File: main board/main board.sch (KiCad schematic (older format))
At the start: 1 part, among them J1 502078-1710

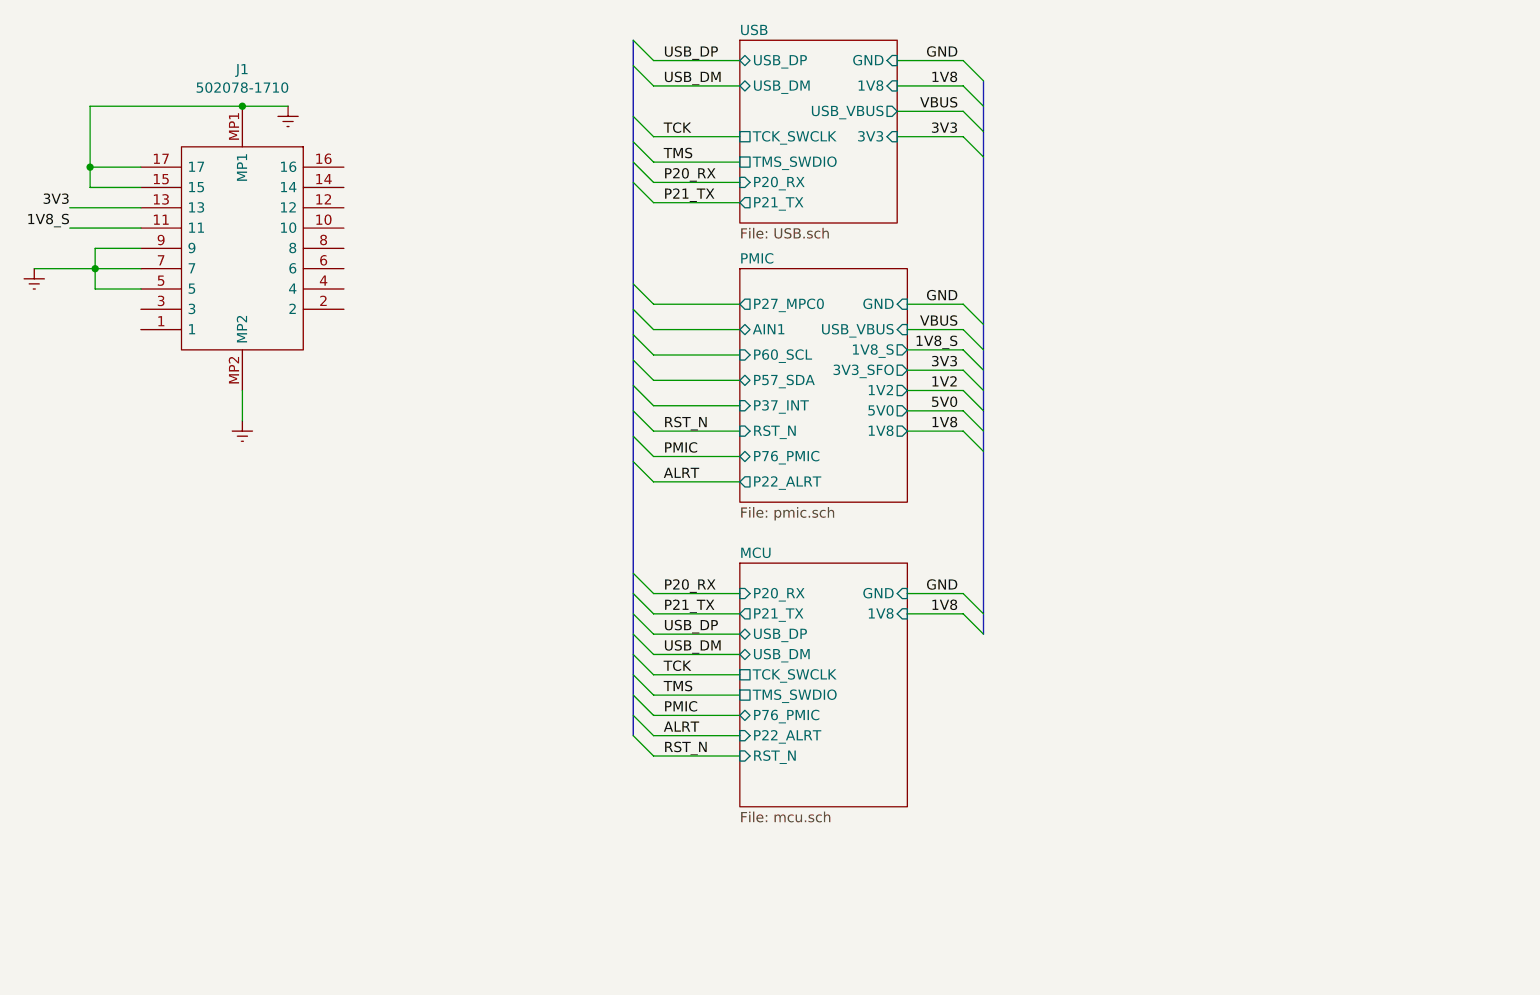
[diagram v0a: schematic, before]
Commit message: added crystal and motion sensor
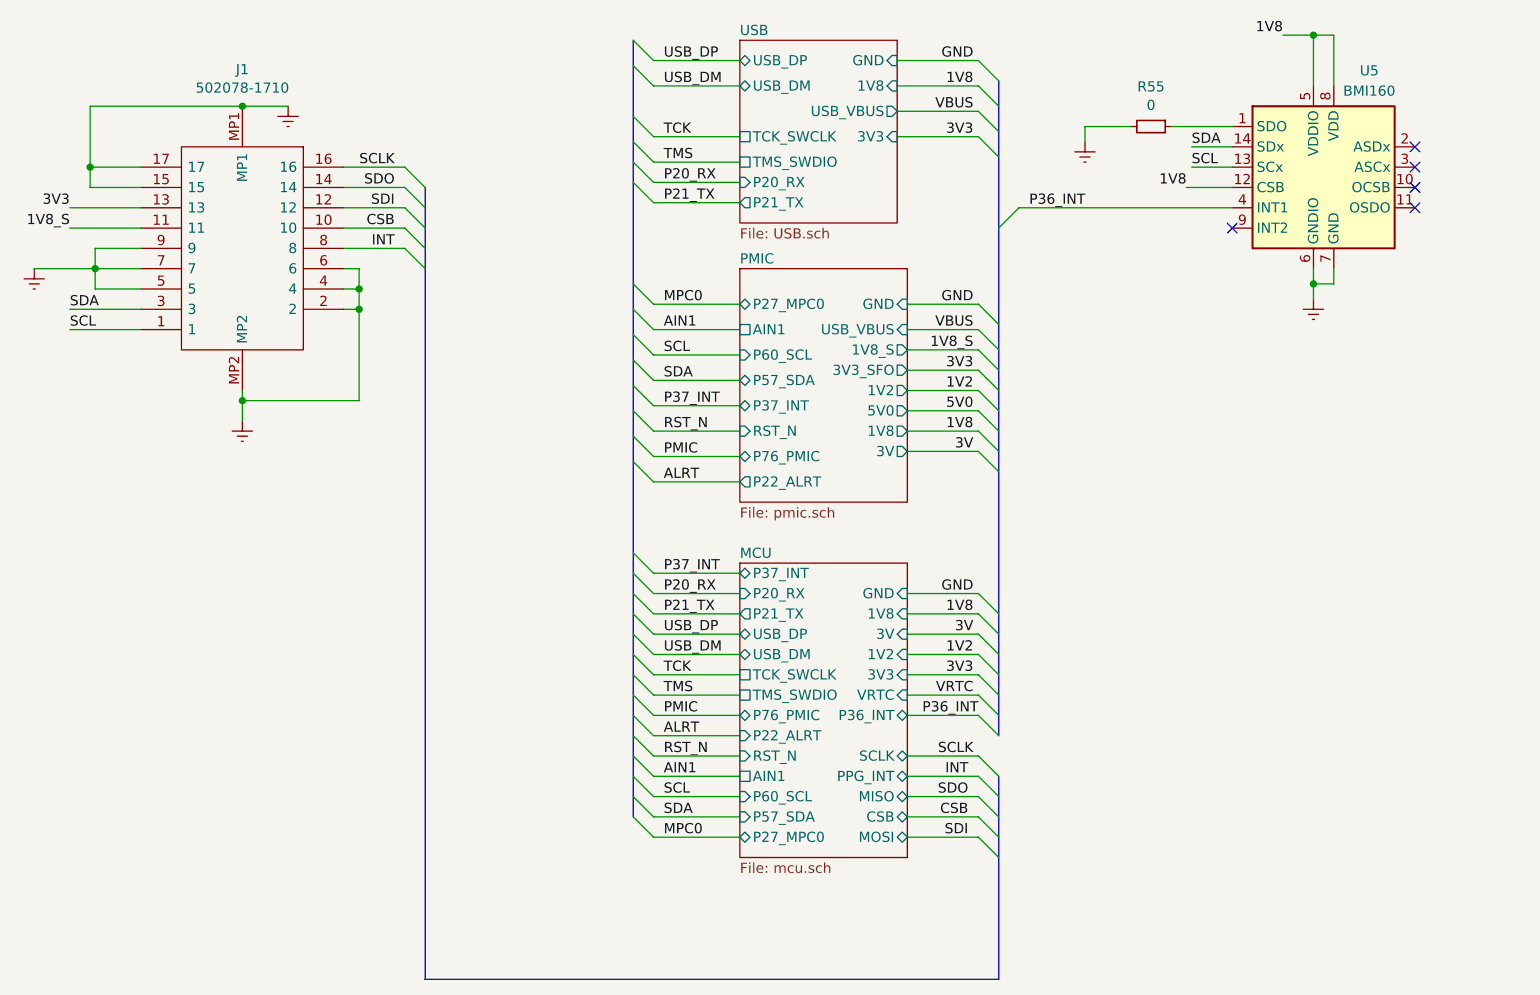
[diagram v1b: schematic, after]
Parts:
- added R55: 0, symbol Device:R_Small
- added U5: BMI160, Package_LGA:Bosch_LGA-14_3x2.5mm_P0.5mm, symbol Sensor_Motion:BMI160
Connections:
- net 1V8: now also U5.12 (CSB), U5.5 (VDDIO), U5.8 (VDD)
- net GNDREF: now also J1.2, J1.4, J1.6, R55.2, U5.6 (GNDIO), U5.7 (GND)
- net SCL: now reaches J1.1
- net SCL: now also U5.13 (SCx)
- net CSB: now reaches J1.10
- net SDI: now reaches J1.12
- net SDO: now reaches J1.14
- net SCLK: now reaches J1.16
- net SDA: now reaches J1.3
- net SDA: now also U5.14 (SDx)
- net INT: now reaches J1.8
- new net: R55.1, U5.1 (SDO)
- new net P36_INT: U5.4 (INT1)
- no-connect marks 0 -> 5

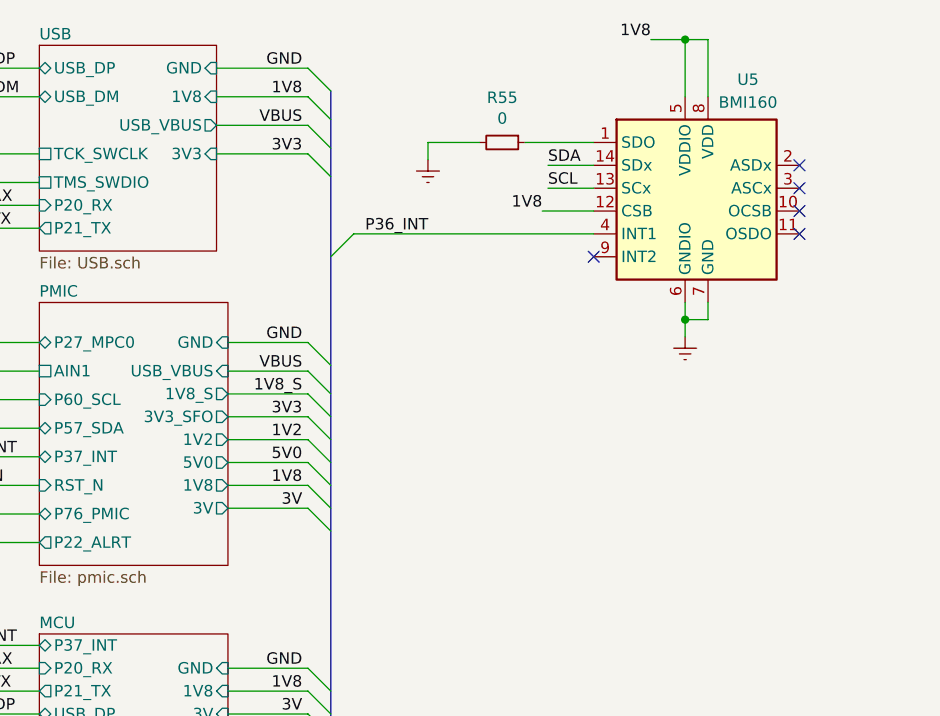
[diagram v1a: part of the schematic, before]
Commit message: added VRTC power input
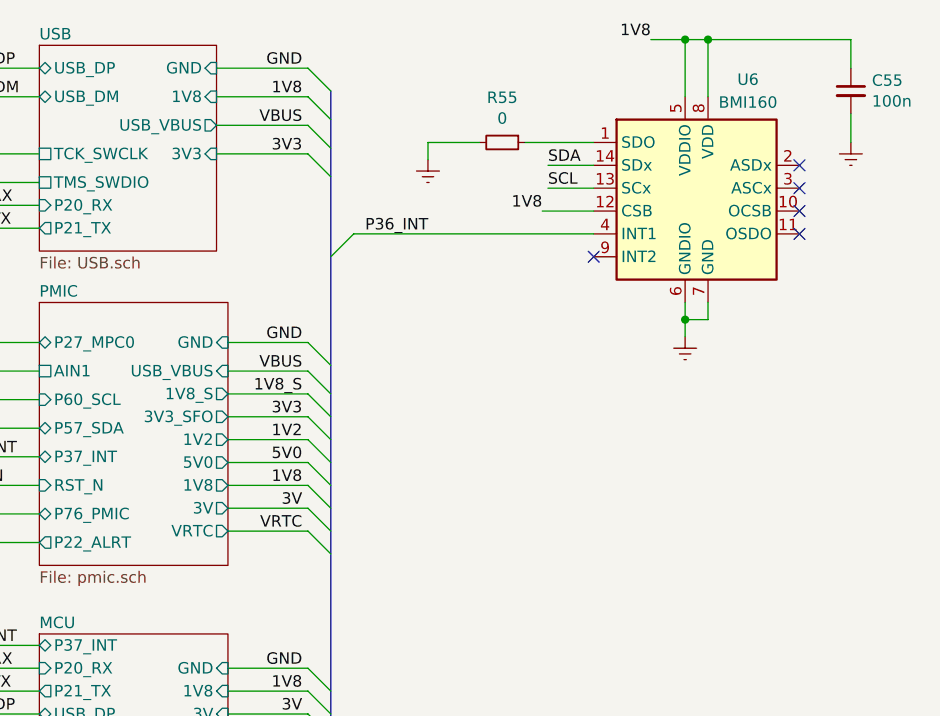
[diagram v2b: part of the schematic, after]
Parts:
- added C55: 100n, symbol Device:C_Small
- renumbered U5 to U6
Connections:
- net 1V8: now also C55.1
- net GNDREF: now also C55.2
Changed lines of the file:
@@
 F16 "P22_ALRT" O L 4500 3050 50
 F17 "3V" O R 5325 2900 50
+F18 "VRTC" O R 5325 3000 50
 $EndSheet
 $Sheet
@@
 CSB
 $Comp
-L Sensor_Motion:BMI160 U5
+L Sensor_Motion:BMI160 U6
 U 1 1 603EB074
 P 7425 1500
-F 0 "U5" H 7600 1975 50  0000 C CNN
+F 0 "U6" H 7600 1975 50  0000 C CNN
 F 1 "BMI160" H 7600 1875 50  0000 C CNN
 F 2 "Package_LGA:Bosch_LGA-14_3x2.5mm_P0.5mm" H 7425 1500 50  0001 C CNN
@@
 Wire Wire Line
 	5325 4800 5675 4800
+$Comp
+L Device:C_Small C55
+U 1 1 604B43E5
+P 8050 1075
+F 0 "C55" H 8142 1121 50  0000 L CNN
+F 1 "100n" H 8142 1030 50  0000 L CNN
+F 2 "" H 8050 1075 50  0001 C CNN
+F 3 "~" H 8050 1075 50  0001 C CNN
+	1    8050 1075
+	1    0    0    -1
+$EndComp
+$Comp
+L power:GNDREF #PWR0163
+U 1 1 604B5731
+P 8050 1300
+F 0 "#PWR0163" H 8050 1050 50  0001 C CNN
+F 1 "GNDREF" H 8250 1200 50  0001 C CNN
+F 2 "" H 8050 1300 50  0001 C CNN
+F 3 "" H 8050 1300 50  0001 C CNN
+	1    8050 1300
+	1    0    0    -1
+$EndComp
+Wire Wire Line
+	8050 1175 8050 1300
+Wire Wire Line
+	8050 975  8050 850
+Wire Wire Line
+	8050 850  7425 850
+Connection ~ 7425 850
+Entry Wire Line
+	5675 3000 5775 3100
+Wire Wire Line
+	5325 3000 5675 3000
+Text Label 5650 3000 2    50   ~ 0
+VRTC
 Wire Bus Line
 	5775 4500 5775 5500

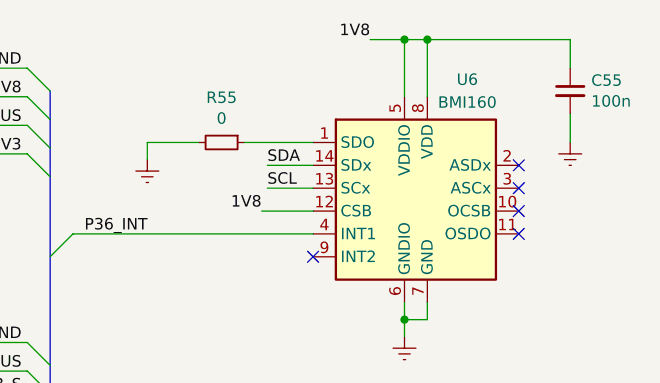
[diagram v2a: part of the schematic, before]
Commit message: added flash and LED
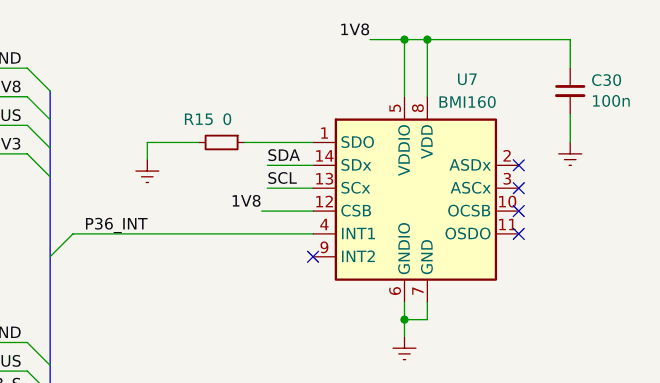
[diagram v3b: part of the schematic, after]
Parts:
- renumbered C55 to C30, R55 to R15, U6 to U7
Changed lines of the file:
@@
 CSB
 $Comp
-L Sensor_Motion:BMI160 U6
+L Sensor_Motion:BMI160 U7
 U 1 1 603EB074
 P 7425 1500
-F 0 "U6" H 7600 1975 50  0000 C CNN
+F 0 "U7" H 7600 1975 50  0000 C CNN
 F 1 "BMI160" H 7600 1875 50  0000 C CNN
 F 2 "Package_LGA:Bosch_LGA-14_3x2.5mm_P0.5mm" H 7425 1500 50  0001 C CNN
@@
 Text Label 5675 4200 2    50   ~ 0
 P36_INT
-$Comp
-L Device:R_Small R55
-U 1 1 6042CEDB
-P 6525 1300
-F 0 "R55" V 6329 1300 50  0000 C CNN
-F 1 "0" V 6420 1300 50  0000 C CNN
-F 2 "" H 6525 1300 50  0001 C CNN
-F 3 "~" H 6525 1300 50  0001 C CNN
-	1    6525 1300
-	0    1    1    0
-$EndComp
 Wire Wire Line
 	6625 1300 6925 1300
@@
 	5325 4800 5675 4800
 $Comp
-L Device:C_Small C55
+L Device:C_Small C30
 U 1 1 604B43E5
 P 8050 1075
-F 0 "C55" H 8142 1121 50  0000 L CNN
+F 0 "C30" H 8142 1121 50  0000 L CNN
 F 1 "100n" H 8142 1030 50  0000 L CNN
 F 2 "" H 8050 1075 50  0001 C CNN
@@
 Text Label 5650 3000 2    50   ~ 0
 VRTC
+$Comp
+L Device:R_Small R15
+U 1 1 6042CEDB
+P 6525 1300
+F 0 "R15" V 6425 1200 50  0000 C CNN
+F 1 "0" V 6425 1325 50  0000 C CNN
+F 2 "" H 6525 1300 50  0001 C CNN
+F 3 "~" H 6525 1300 50  0001 C CNN
+	1    6525 1300
+	0    1    1    0
+$EndComp
 Wire Bus Line
 	5775 4500 5775 5500

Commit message: add some part numbers to main board
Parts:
- J1: Digikey Part Number (none) -> WM14446TR-ND; Price (none) -> 1.68
- R15: footprint (none) -> Resistor_SMD:R_0402_1005Metric; Digikey Part Number (none) -> 541-4062-2-ND; Mouser Price/Stock (none) -> https://www.mouser.ee/ProductDetail/Vishay-Dale/CRCW0402000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; Price (none) -> 0.09
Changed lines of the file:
@@
 F 8 "Molex" H 3300 900 50  0001 L CNN "Manufacturer_Name"
 F 9 "502078-1710" H 3300 800 50  0001 L CNN "Manufacturer_Part_Number"
+F 10 "WM14446TR-ND" V 2050 1200 50  0001 C CNN "Digikey Part Number"
+F 11 "1.68" V 2050 1200 50  0001 C CNN "Price"
 	1    2050 1200
 	0    1    1    0
@@
 F 0 "R15" V 6425 1200 50  0000 C CNN
 F 1 "0" V 6425 1325 50  0000 C CNN
-F 2 "" H 6525 1300 50  0001 C CNN
-F 3 "~" H 6525 1300 50  0001 C CNN
+F 2 "Resistor_SMD:R_0402_1005Metric" H 6525 1300 50  0001 C CNN
+F 3 "https://www.mouser.ee/datasheet/2/427/crcwce3-1762584.pdf" H 6525 1300 50  0001 C CNN
+F 4 "https://www.mouser.ee/ProductDetail/Vishay-Dale/CRCW04020000Z0EDC/?qs=sGAEpiMZZMvdGkrng054t0DrEhLhGh8gwkqbMx2gSI%252BmKUnjnIW1MQ%3D%3D" V 6525 1300 50  0001 C CNN "Mouser Price/Stock"
+F 5 "541-4062-2-ND" V 6525 1300 50  0001 C CNN "Digikey Part Number"
+F 6 "0.09" V 6525 1300 50  0001 C CNN "Price"
 	1    6525 1300
 	0    1    1    0

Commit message: added 100n capacitor
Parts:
- C30: footprint (none) -> Capacitor_SMD:C_0402_1005Metric; Digikey Part Number (none) -> 311-3340-2-ND; Mouser Price/Stock (none) -> https://www.mouser.ee/ProductDetail/Yageo/CC0402KRX5R5BB104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; Price (none) -> 0.09
- U7: Digikey Part Number (none) -> 828-1057-2-ND; Mouser Price/Stock (none) -> https://www.mouser.ee/ProductDetail/Bosch-Sensortec/BMI160/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; Price (none) -> 3.75
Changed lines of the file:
@@
 F 1 "BMI160" H 7600 1875 50  0000 C CNN
 F 2 "Package_LGA:Bosch_LGA-14_3x2.5mm_P0.5mm" H 7425 1500 50  0001 C CNN
-F 3 "https://ae-bst.resource.bosch.com/media/_tech/media/datasheets/BST-BMI160-DS000.pdf" H 6725 2350 50  0001 C CNN
+F 3 "https://www.mouser.ee/datasheet/2/783/BST_BMI160_DS000-1509569.pdf" H 6725 2350 50  0001 C CNN
+F 4 "https://www.mouser.ee/ProductDetail/Bosch-Sensortec/BMI160/?qs=Lj1LZLjqIN1DEsUDgjehlg%3D%3D" H 7425 1500 50  0001 C CNN "Mouser Price/Stock"
+F 5 "828-1057-2-ND" H 7425 1500 50  0001 C CNN "Digikey Part Number"
+F 6 "3.75" H 7425 1500 50  0001 C CNN "Price"
 	1    7425 1500
 	1    0    0    -1
@@
 F 0 "C30" H 8142 1121 50  0000 L CNN
 F 1 "100n" H 8142 1030 50  0000 L CNN
-F 2 "" H 8050 1075 50  0001 C CNN
-F 3 "~" H 8050 1075 50  0001 C CNN
+F 2 "Capacitor_SMD:C_0402_1005Metric" H 8050 1075 50  0001 C CNN
+F 3 "https://www.mouser.ee/datasheet/2/447/UPY_GPHC_X5R_4V_to_50V_25-1131599.pdf" H 8050 1075 50  0001 C CNN
+F 4 "https://www.mouser.ee/ProductDetail/Yageo/CC0402KRX5R5BB104/?qs=T%2F3nPWKqOSbG4z8ii3LyCg%3D%3D" H 8050 1075 50  0001 C CNN "Mouser Price/Stock"
+F 5 "311-3340-2-ND" H 8050 1075 50  0001 C CNN "Digikey Part Number"
+F 6 "0.09" H 8050 1075 50  0001 C CNN "Price"
 	1    8050 1075
 	1    0    0    -1

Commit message: mcu parts
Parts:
- renumbered C30 to C31
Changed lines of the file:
@@
 	5325 4800 5675 4800
 $Comp
-L Device:C_Small C30
+L Device:C_Small C31
 U 1 1 604B43E5
 P 8050 1075
-F 0 "C30" H 8142 1121 50  0000 L CNN
+F 0 "C31" H 8142 1121 50  0000 L CNN
 F 1 "100n" H 8142 1030 50  0000 L CNN
 F 2 "Capacitor_SMD:C_0402_1005Metric" H 8050 1075 50  0001 C CNN
